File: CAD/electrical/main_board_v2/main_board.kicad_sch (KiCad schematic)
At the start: 41 parts, among them J10 I2C Motor, J11 JTAG, J12 UART PGM, J13 RS485, J14 RS485, J3 Trigger, J4 Side select, J7 I2C Peripheral, J8 I2C Peripheral, J9 I2C Motor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

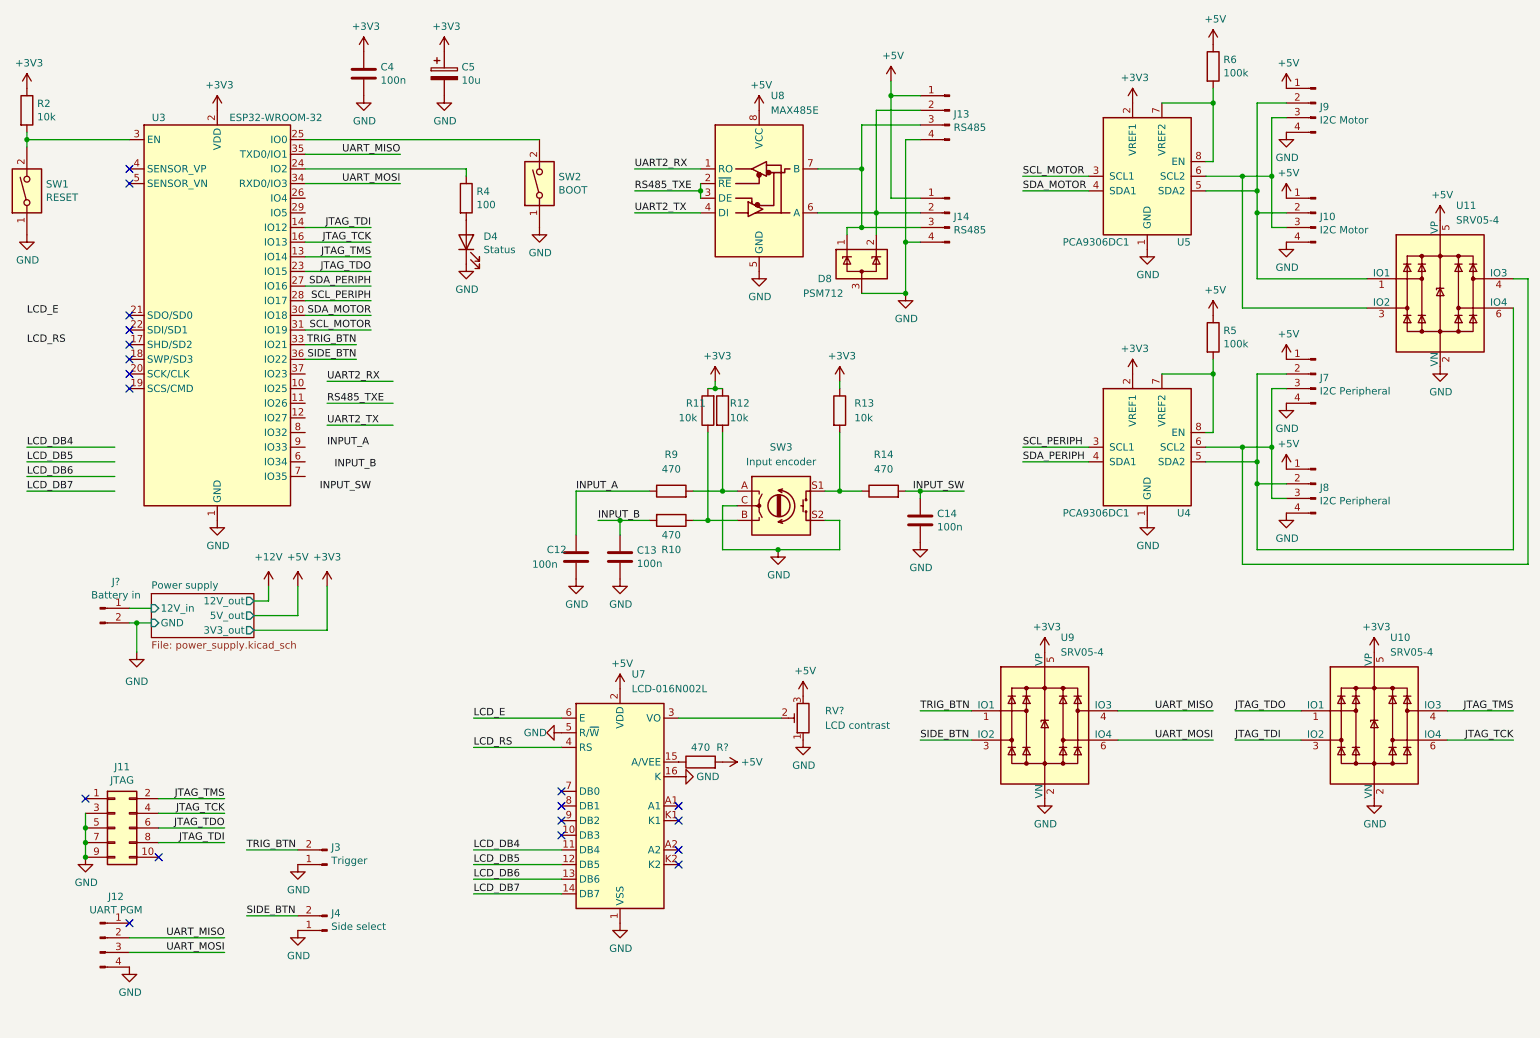
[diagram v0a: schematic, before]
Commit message: Updated version of motor board and main board
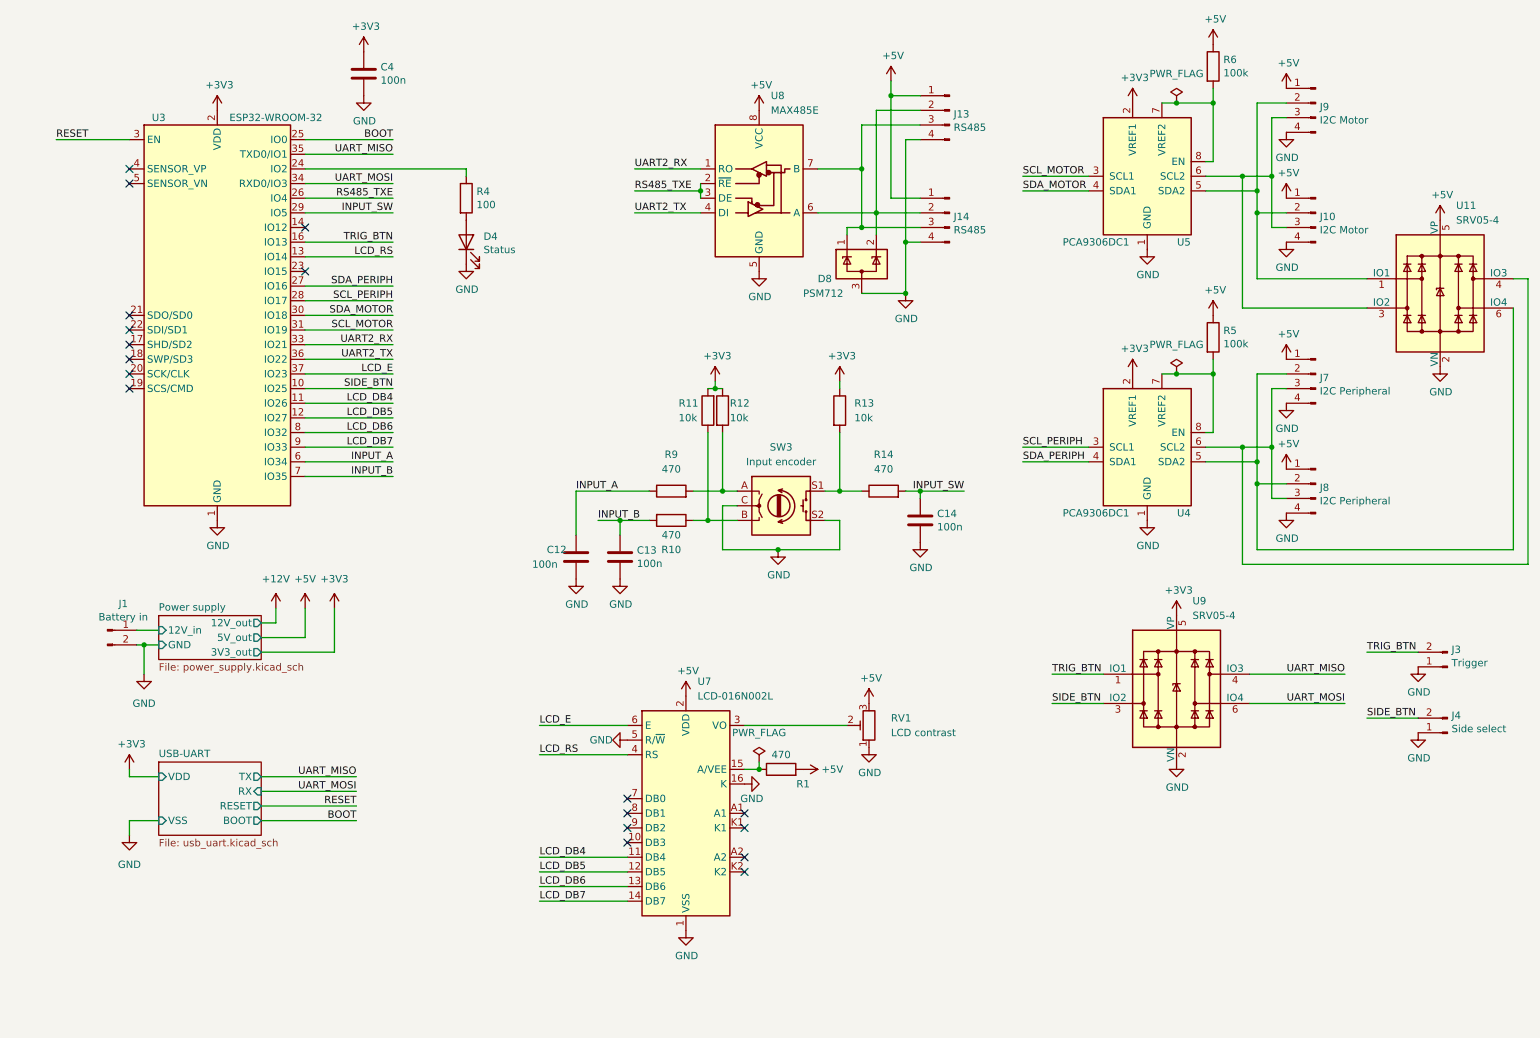
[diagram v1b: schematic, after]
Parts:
- removed C5: 10u, Capacitor_THT:CP_Radial_D6.3mm_P2.50mm, symbol main_board-rescue:CP-Device
- removed J11: JTAG, Connector_IDC:IDC-Header_2x05_P2.54mm_Vertical, symbol Connector_Generic:Conn_02x05_Odd_Even
- removed J12: UART PGM, Connector_Molex:Molex_KK-254_AE-6410-04A_1x04_P2.54mm_Vertical, symbol Connector:Conn_01x04_Male
- removed R2: 10k, Resistor_SMD:R_1206_3216Metric, symbol Device:R
- removed SW1: RESET, Button_Switch_THT:SW_PUSH_6mm, symbol Switch:SW_DIP_x01
- removed SW2: BOOT, Button_Switch_THT:SW_PUSH_6mm, symbol Switch:SW_DIP_x01
- removed U10: SRV05-4, Package_TO_SOT_SMD:SOT-23-6, symbol Power_Protection:SRV05-4
- R1: renamed from R?; footprint (none) -> Resistor_SMD:R_1206_3216Metric
- R10, R11, R12, R13, R14, R9: footprint (none) -> Resistor_SMD:R_0603_1608Metric
- R5, R6: footprint Resistor_SMD:R_1206_3216Metric -> Resistor_SMD:R_0603_1608Metric
- RV1: renamed from RV?; footprint (none) -> Potentiometer_THT:Potentiometer_Piher_PT-10-V05_Vertical
- SW3: footprint (none) -> Rotary_Encoder:RotaryEncoder_Alps_EC11E-Switch_Vertical_H20mm
- U8: footprint (none) -> Package_SO:SOIC-8_3.9x4.9mm_P1.27mm
- gave numbers to parts that had none: 1
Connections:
- net JTAG_TCK is gone; now on net TRIG_BTN: U3.16 (IO13)
- net JTAG_TMS is gone; now on net LCD_RS: U3.13 (IO14)
- net INPUT_A: now also U3.6 (IO34)
- net INPUT_B: now also U3.7 (IO35)
- net INPUT_SW: now also U3.29 (IO5)
- net LCD_DB4: now also U3.11 (IO26)
- net LCD_DB5: now also U3.12 (IO27)
- net LCD_DB6: now also U3.8 (IO32)
- net LCD_DB7: now also U3.9 (IO33)
- net LCD_E: now also U3.37 (IO23)
- net RS485_TXE: now also U3.26 (IO4)
- net SIDE_BTN: now also U3.10 (IO25); no longer U3.36 (IO22)
- net TRIG_BTN: no longer U3.33 (IO21)
- net UART2_RX: now also U3.33 (IO21)
- net UART2_TX: now also U3.36 (IO22)
- net BOOT: now reaches U3.25 (IO0)
- net RESET: now reaches U3.3 (EN)
- net JTAG_TDI: no longer names the net of U3.14 (IO12)
- net JTAG_TDO: no longer names the net of U3.23 (IO15)
- no-connect marks 19 -> 18
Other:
- added sheet USB-UART (usb_uart.kicad_sch)
- moved on the sheet: J1, J3, J4, R1, RV1, U7, U9

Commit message: Kicad CAD for mainboard and motorboard (final)
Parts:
- added J2: UART PGM, Connector_Molex:Molex_KK-254_AE-6410-04A_1x04_P2.54mm_Vertical, symbol Connector:Conn_01x04_Male
- added R2, R3: 1k, Resistor_SMD:R_0603_1608Metric, symbol Device:R
- R4: value 100 -> 470
- R5, R6: value 100k -> 33k
- RV1: footprint Potentiometer_THT:Potentiometer_Piher_PT-10-V05_Vertical -> Potentiometer_SMD:Potentiometer_Bourns_3314J_Vertical
- U3: footprint RF_Module:ESP32-WROOM-32 -> RF_Module:ESP32-WROOM-32U
- U7: footprint Display:LCD-016N002L -> Display:WC1602A
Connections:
- net +5V: now also R2.1
- net GND: now also J2.4 (Pin_4), R3.2
- net at D8.1 (K), J13.3 (Pin_3), J14.3 (Pin_3)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: now also R3.1
- net at D8.2 (K), J13.2 (Pin_2), J14.2 (Pin_2)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: now also R2.2
- net UART_MISO renamed UART_TX
- net UART_TX: now also J2.2 (Pin_2)
- net UART_MOSI renamed UART_RX
- net UART_RX: now also J2.3 (Pin_3)
- no-connect marks 18 -> 19
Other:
- note added: "Attention ESP32 pas vraiment 5V tolerant!!!"
- note added: "Trous de l'écran trop petits"
- moved on the sheet: U8

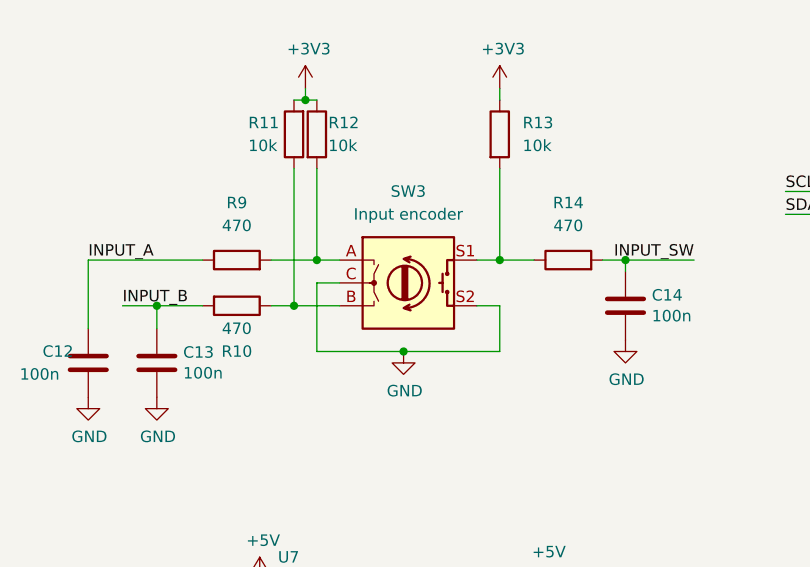
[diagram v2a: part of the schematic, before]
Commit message: LD06 board colplet
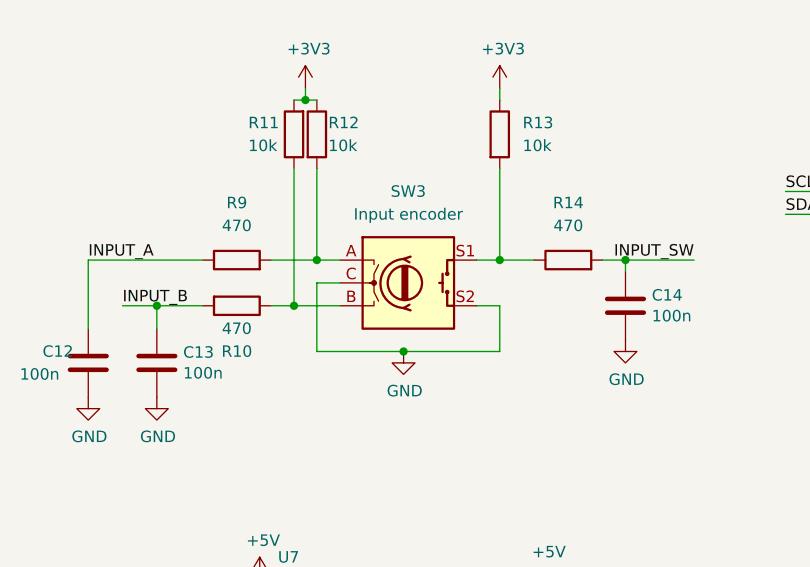
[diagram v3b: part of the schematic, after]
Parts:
- D4: LCSC C72038 -> C2286
- R2: LCSC (none) -> C20190
- R3: LCSC (none) -> C20192
